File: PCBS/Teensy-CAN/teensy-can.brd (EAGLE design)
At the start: 25.5 x 48.4 mm, 12 parts

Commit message: Adding DC-DC to control board. UNFINISHED
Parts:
- added C1, C2, C3, C4: (no value), rcl:C0402
- added GND, GND2, VIN: (no value), wirepad:1,6/0,8
- added U1: AP1509-50SG-13, AP150950SG13:SOP-8L_DIO
- moved PRECHRG-RLY 0.28 mm to (24.1, 26.5)
- moved CONTACT-RL 0.25 mm to (24.1, 29.1)
- moved TFT_RST 0.13 mm to (1.91, 29.1)
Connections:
- new net N$10: GND.1, U$2.GND@1, U$2.GND@2
- new net N$11: C3.1, C4.1, U1.1, VIN.1
- new net N$12: C1.1, C2.1, U$2.VIN, U1.2, U1.3
- net GND: now also C1.2, C2.2, C3.2, C4.2, GND2.1, U1.4, U1.5, U1.6, U1.7, U1.8; no longer U$2.GND@1, U$2.GND@2
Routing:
- net N$12: track 0.00 -> 88.2 mm, vias 0 -> 3
- net GND: track 13.1 -> 55.6 mm
- net N$10: track 0.00 -> 15.0 mm
- net N$11: track 0.00 -> 12.2 mm
- net N$5: track 11.8 -> 10.8 mm
- added copper zone on layer 1, net GND
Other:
- board size 25.5 x 48.4 mm -> 28 x 47.2 mm

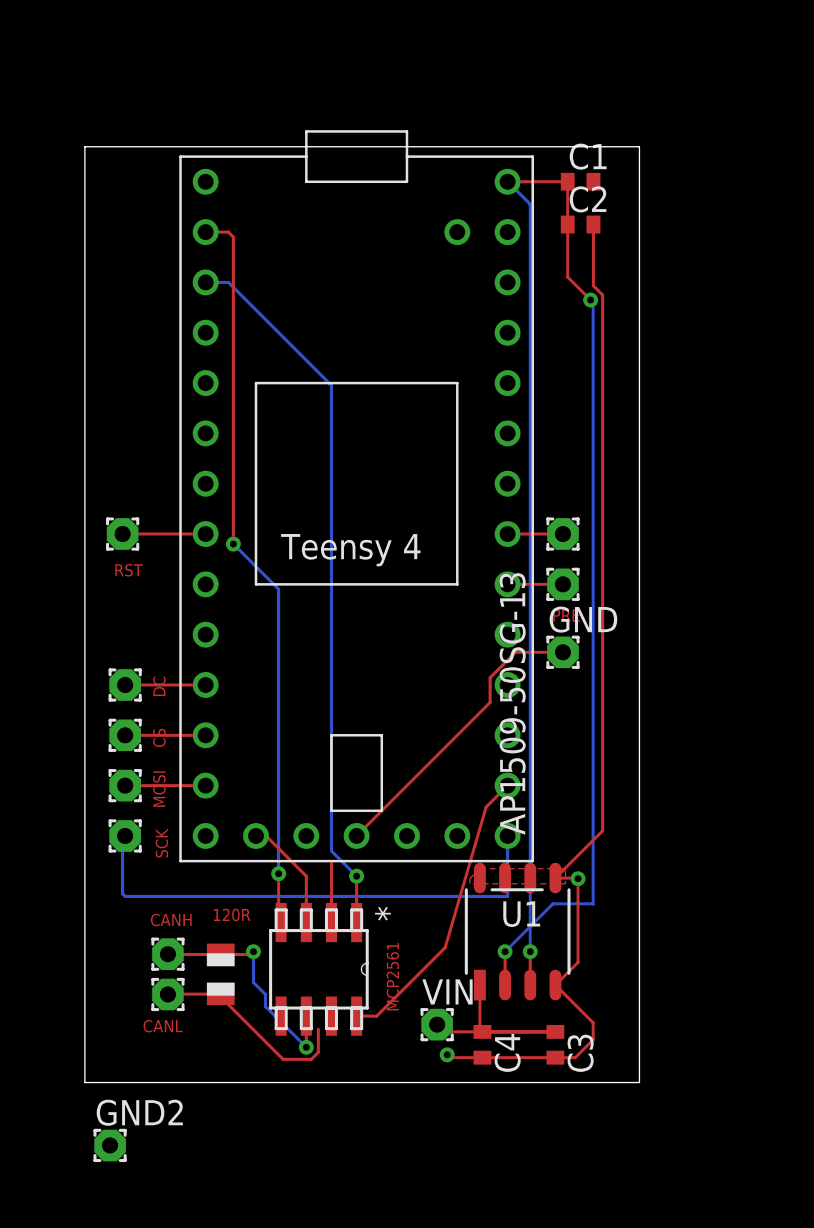
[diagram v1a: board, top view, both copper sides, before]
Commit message: teensy board final draft
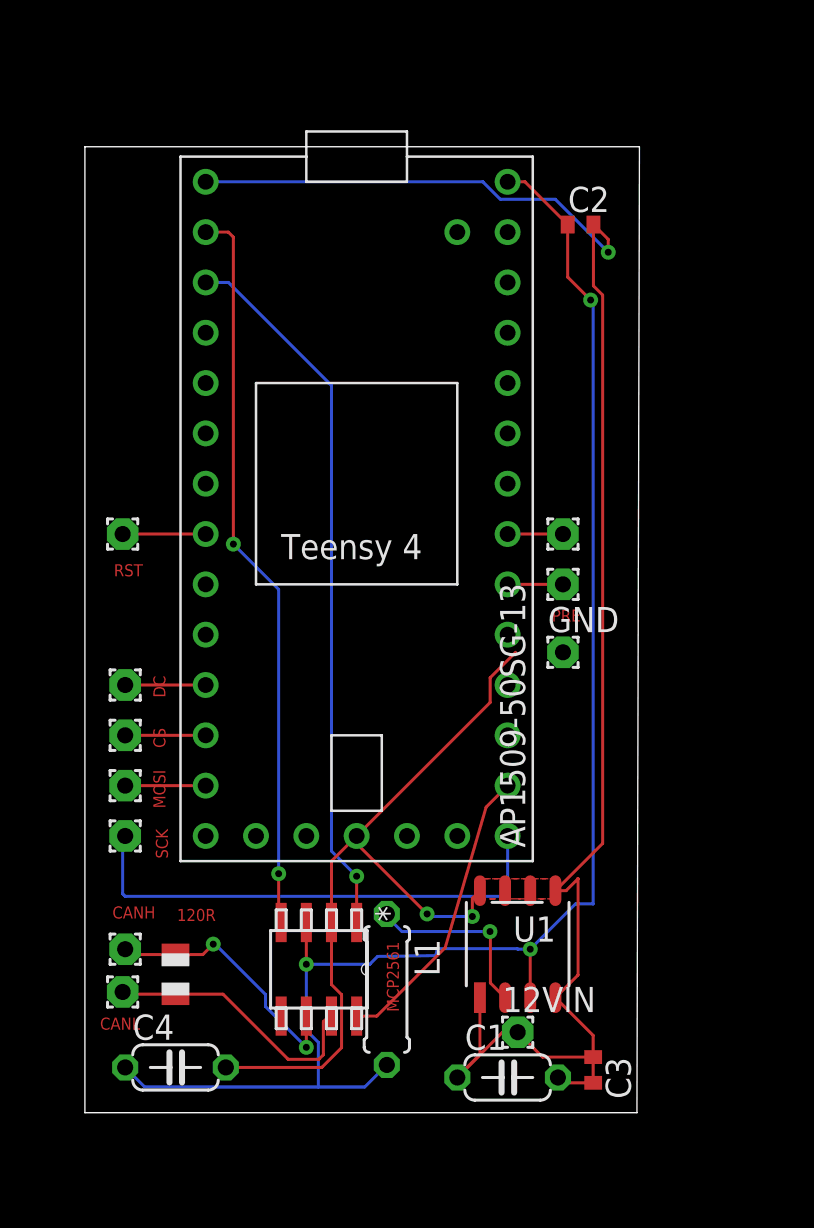
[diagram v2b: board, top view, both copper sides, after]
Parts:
- removed GND2, VIN: (no value), wirepad:1,6/0,8
- added 12VIN: (no value), wirepad:1,6/0,8
- added L1: 47uf, rcl:0207/7
- C1, C4: value (none) -> 10uf; device rcl:C0402 -> rcl:C050-024X044
- C2, C3: value (none) -> 0.1uF
- moved C1 45.4 mm to (21.3, 1.65)
- moved C4 15.5 mm to (4.57, 2.16), turned to 0 degrees
- moved C3 2.29 mm to (25.7, 2.03)
- moved CAN_H 2.29 mm to (1.91, 5.97)
- moved 120R 2.29 mm to (4.57, 6.86)
- moved CAN_L 2.17 mm to (2.03, 8.13)
- moved U1 0.63 mm to (21.8, 8.38)
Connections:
- removed net N$10: GND.1, U$2.GND@1, U$2.GND@2
- removed net N$11: C3.1, C4.1, U1.1, VIN.1
- removed net N$12: C1.1, C2.1, U$2.VIN, U1.2, U1.3
- removed net VBAT: U$1.3, U$2.VBAT
- new net 12VIN: 12VIN.1, C1.1, C3.1, U1.1
- new net 5VIN: C2.1, C4.1, L1.2, U$1.3, U$2.VIN, U1.3
- new net OUTPUT: L1.1, U1.2
- net GND: now also GND.1, U$2.GND@1, U$2.GND@2; no longer GND2.1
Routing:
- net N$12: track 88.2 -> 0.00 mm, vias 3 -> 0
- net 5VIN: track 0.00 -> 79.7 mm, vias 0 -> 3
- net GND: track 55.6 -> 112.6 mm, vias 2 -> 3
- net N$10: track 15.0 -> 0.00 mm
- net 12VIN: track 0.00 -> 12.8 mm
- net N$11: track 12.2 -> 0.00 mm
- net OUTPUT: track 0.00 -> 9.30 mm, vias 0 -> 1
- net VBAT: track 5.72 -> 0.00 mm
- net N$5: track 10.8 -> 14.3 mm
- net N$6: track 11.9 -> 13.6 mm
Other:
- board size 28 x 47.2 mm -> 28 x 48.8 mm

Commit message: charger and board changes, adding firmware soon
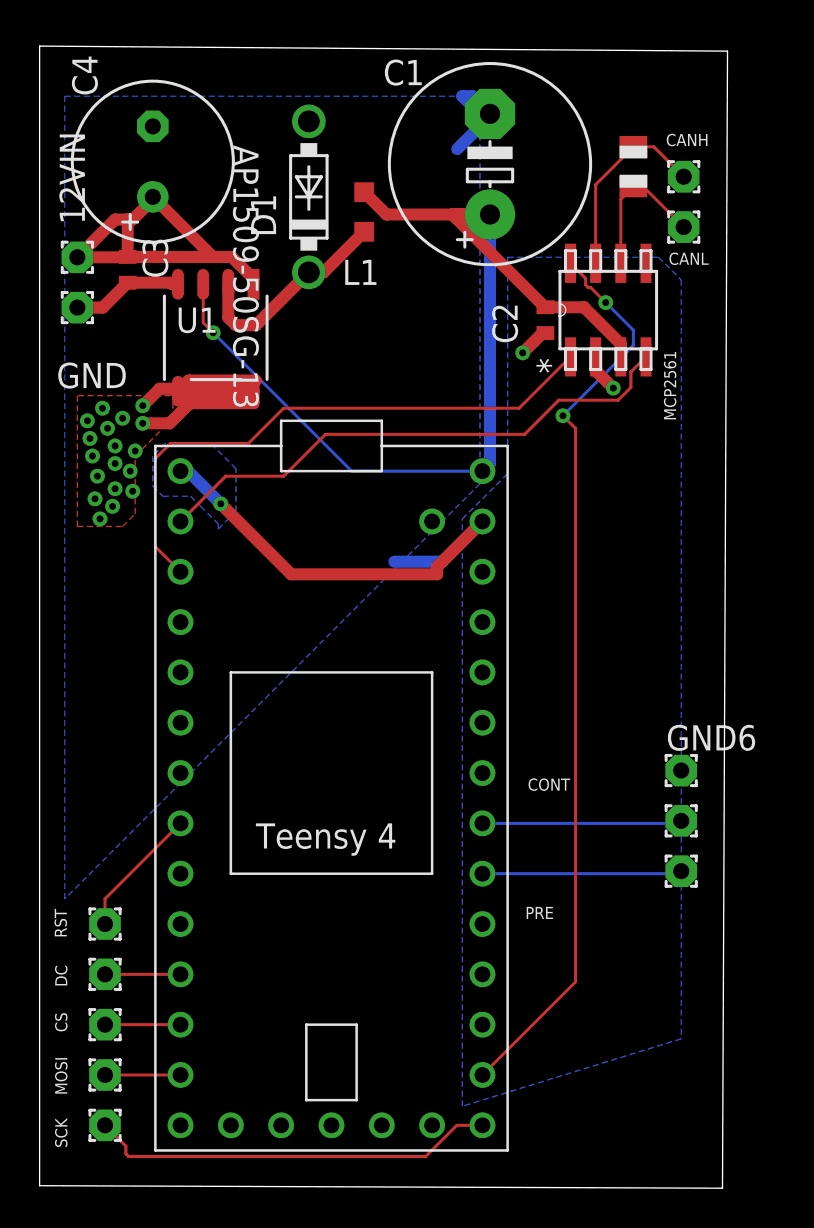
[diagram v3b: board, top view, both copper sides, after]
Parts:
- added D1: 1N5817-T, diode:DO41-7.6
- added GND6: (no value), wirepad:1,6/0,8
- C1: value 10uf -> 1000uF; device rcl:C050-024X044 -> rcl:E5-10,5
- C4: value 10uf -> 330uF; device rcl:C050-024X044 -> rcl:E3,5-8
- L1: value 47uf -> 33uH; device rcl:0207/7 -> rcl:L2012C
- moved CAN_H 50.0 mm to (30.2, 47.1), turned to 0 degrees
- moved 120R 46.9 mm to (27.7, 47.6), turned to 270 degrees
- moved C3 46.7 mm to (2.16, 42.4)
- moved C1 46.1 mm to (20.4, 47.8), turned to 90 degrees
- moved CAN_L 46.1 mm to (30.2, 44.6), turned to 180 degrees
- moved C4 45.7 mm to (3.43, 47.9), turned to 90 degrees
- moved 12VIN 45.0 mm to (-0.38, 43.1), turned to 180 degrees
- moved L1 39.3 mm to (14.1, 45.3), turned to 90 degrees
- moved U$1 36.3 mm to (26.4, 40.4), turned to 90 degrees
- moved U1 34.2 mm to (6.60, 39.0), turned to 270 degrees
- moved GND 30.1 mm to (-0.38, 40.5), turned to 180 degrees
- moved TFT_RST 19.7 mm to (1.02, 9.40)
- moved PRECHRG-RLY 15.7 mm to (30.1, 12.1)
- moved CONTACT-RL 15.7 mm to (30.1, 14.6)
- moved U$2 14.7 mm to (12.4, 17.0)
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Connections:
- net 12VIN: now also C4.+; no longer C1.1
- net 5VIN: now also C1.+; no longer C4.1
- net GND: now also C1.-, C4.-, D1.A, GND6.1, U$2.AGND; no longer C1.2, C4.2
- net OUTPUT: now also D1.C
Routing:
- net GND: track 112.6 -> 59.3 mm, vias 3 -> 21
- net N$4: track 14.8 -> 46.0 mm, vias 0 -> 2
- net 5VIN: track 79.7 -> 52.8 mm, vias 3 -> 1
- net CANRX: track 37.1 -> 27.4 mm, vias 2 -> 0
- net 12VIN: track 12.8 -> 21.0 mm
- net N$2: track 2.79 -> 10.1 mm
- net N$1: track 2.79 -> 10.1 mm
- net CANTX: track 36.1 -> 29.3 mm, vias 1 -> 0
- net N$6: track 13.6 -> 7.53 mm, vias 2 -> 0
- net N$9: track 25.5 -> 20.6 mm
- net N$5: track 14.3 -> 9.83 mm
- net N$3: track 4.19 -> 6.66 mm
- net OUTPUT: track 9.30 -> 10.7 mm, vias 1 -> 0
- added copper zone on layer 16, net GND
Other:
- board size 28 x 48.8 mm -> 34.7 x 57.6 mm
- board text added: "CONT"
- board text removed: "120R"
